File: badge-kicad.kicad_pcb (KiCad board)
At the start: 2 copper layers, 152.7 x 76.7 mm, 126 parts, among them J2 JTAG, P2 CONN_02X20, P3 FTDI BACKUP, P4 USB_MICRO_RIGHT, P5 LED OUT (DNP), SW1 RESET, SW2 POWERON, SW3 TM1000, SW4 UP, SW5 DN, SW6 LEFT, SW7 RIGHT, SW8 ENTER, U1 WS2812B, U10 WS2812B, U11 WS2812B, U12 WS2812B, U13 MKW01Z128, U14 FT232RL SSOP, U15 MF-REG-SOT235-3.3V-300mA, U16 MCP73831T-2ACI/OT, U18 LM386, U2 WS2812B, U3 WS2812B, U4 WS2812B, U5 WS2812B, U6 WS2812B, U7 WS2812B, U8 WS2812B, U9 WS2812B, Y1 EXS00A-CS02368

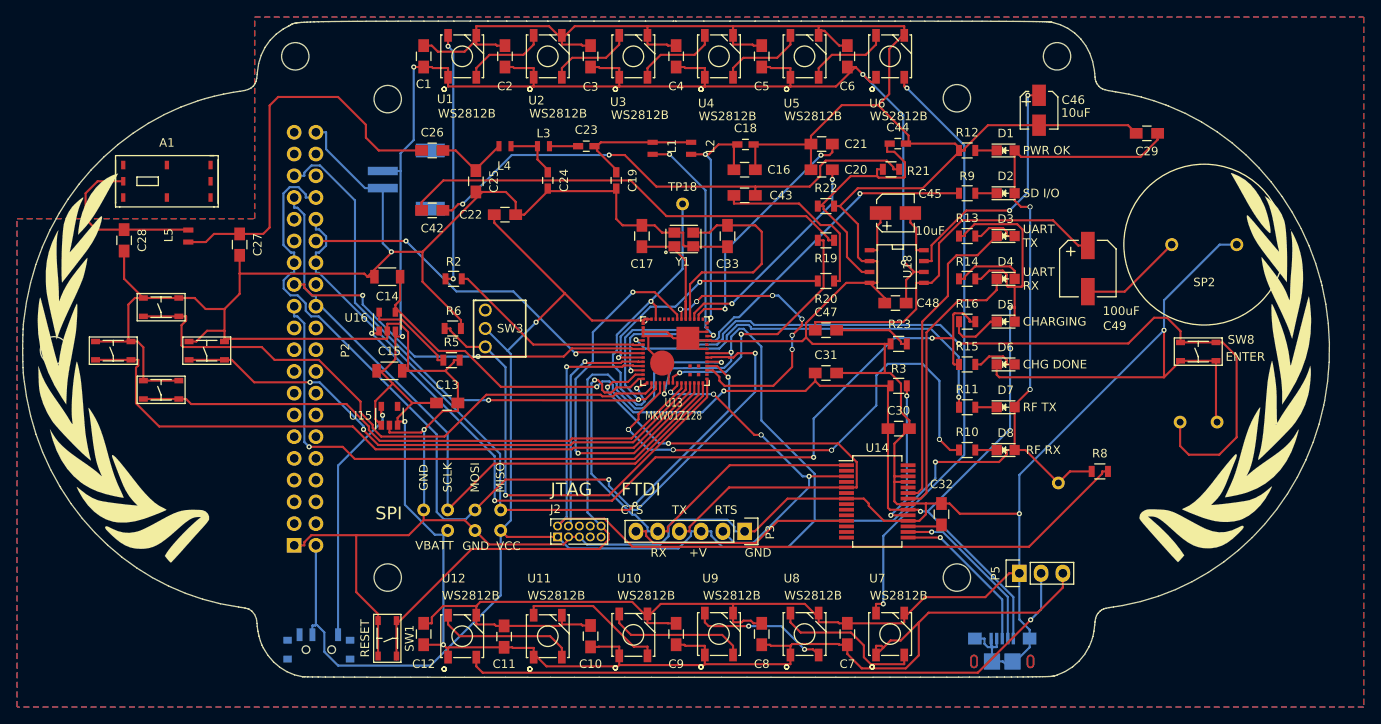
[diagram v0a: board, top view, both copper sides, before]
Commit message: Revision 2 final layout.
Add connection for missing VBAT connector, add some decoupling caps on KW01
Output drill files again.
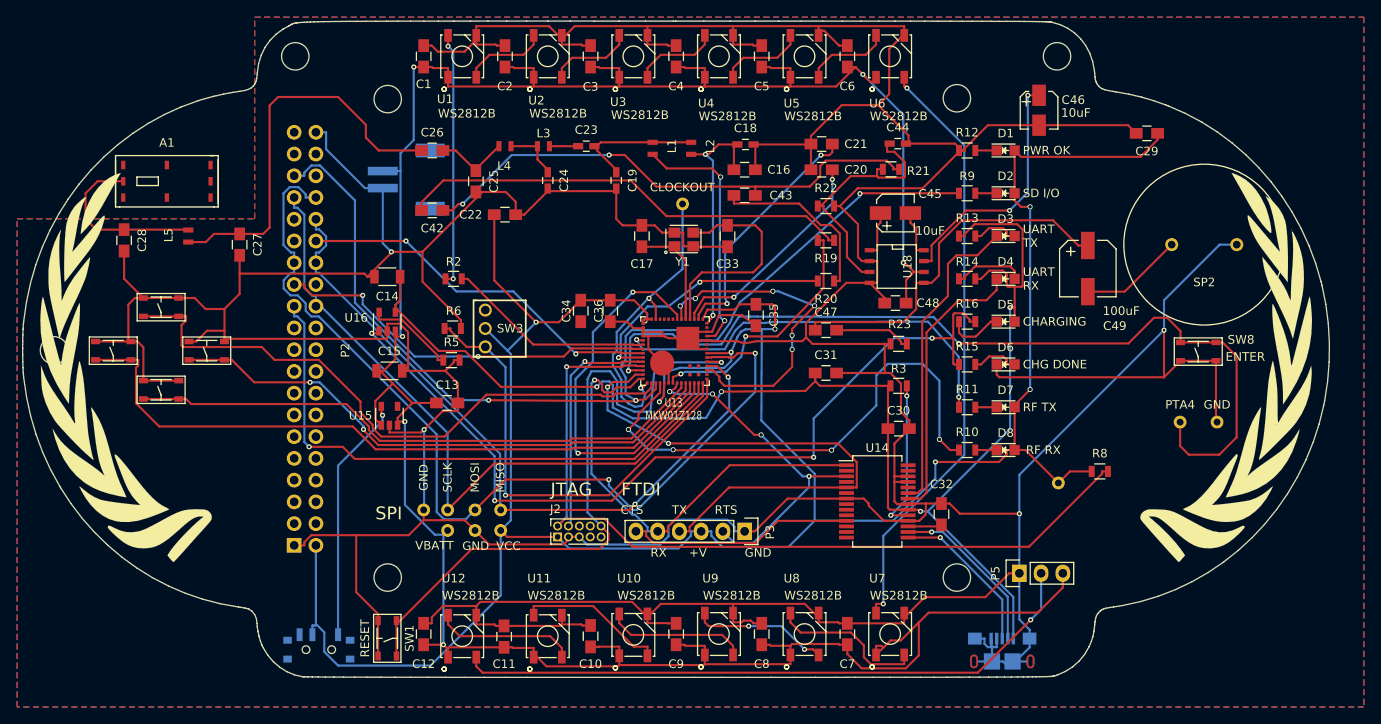
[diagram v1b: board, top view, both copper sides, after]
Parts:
- added C34: 0.1uF, Capacitors_SMD:C_0805_HandSoldering, F.Cu at (141.3, 84.5)
- added C35: 0.1uF, Capacitors_SMD:C_0805_HandSoldering, F.Cu at (158.4, 85.0)
- added C36: 0.1uF, Capacitors_SMD:C_0805_HandSoldering, F.Cu at (137.9, 84.5)
- moved ? 0.32 mm to (82.7, 91.0)
- moved ? 0.10 mm to (215.3, 91.0)
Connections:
- U13 pad 43: Net-(U13-Pad43) -> VCC
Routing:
- net VCC: track 287.2 -> 306.0 mm, vias 6 -> 7
- net GND: track 820.7 -> 835.8 mm
- net RF_RESET: track 35.2 -> 38.5 mm
- net Net-(L1-Pad1): track 26.0 -> 29.3 mm
- net RESET_TGTMCU: track 77.3 -> 79.8 mm
- net VUSB: track 164.0 -> 165.9 mm
- net SWENTER: track 103.4 -> 104.3 mm
- net UART_TX: track 64.0 -> 64.6 mm
- net PTB0: track 118.0 -> 118.5 mm
- net PWM_SOUND: track 30.3 -> 29.7 mm
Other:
- board text added: "CLOCKOUT"
- board text added: "PTA4"
- board text added: "SPQR - The Ides of March - Revision 2 DEFCON 25 (2017) John Adams @netik (PCB, HW, SW) Bill Paul (Drivers, Board bringup, HW, SW) Egan Hirvela (Game Mechanics) Matthew Harris (Art, Character Design) Based on ChbiOS RTC HAIL CASEAR! Made in San Francisco https://retina.net/spqr"
- board text removed: "SPQR - The Ides of March - Revision 2 DEFCON 25 (2017) John Adams @netik (PCB, HW, SW) Bill Paul (Drivers, Board bringup, HW SW) Egan Hirvela (Game Mechanics) Matthew Harris (Art, Character Design) Based on ChbiOS RTC HAIL CASEAR! Made in San Francisco"
